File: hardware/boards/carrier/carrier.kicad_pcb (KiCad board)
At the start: 4 copper layers, 106 x 34.3 mm, 50 parts, among them J1 XT30PW(2+2), Q1 IPB020N10N5LF, Q2 2N7002, Q3 2N7002, U1 STM32G031G6U6, U2 LM5163DDAR, U3 LMX5069MS, U4 INA237AIDGSR

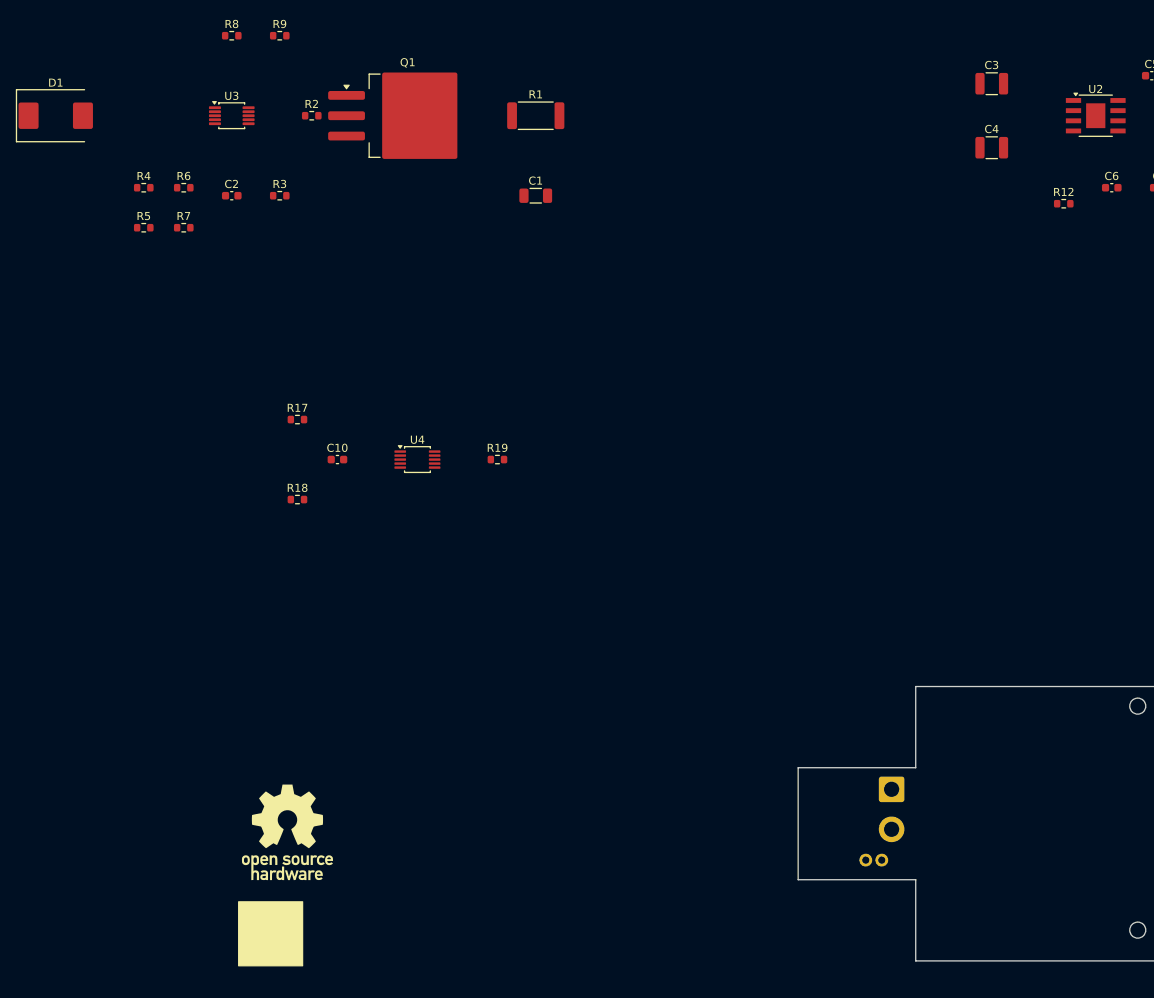
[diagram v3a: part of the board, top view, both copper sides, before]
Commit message: hardware: place carrier input protection and hot-swap
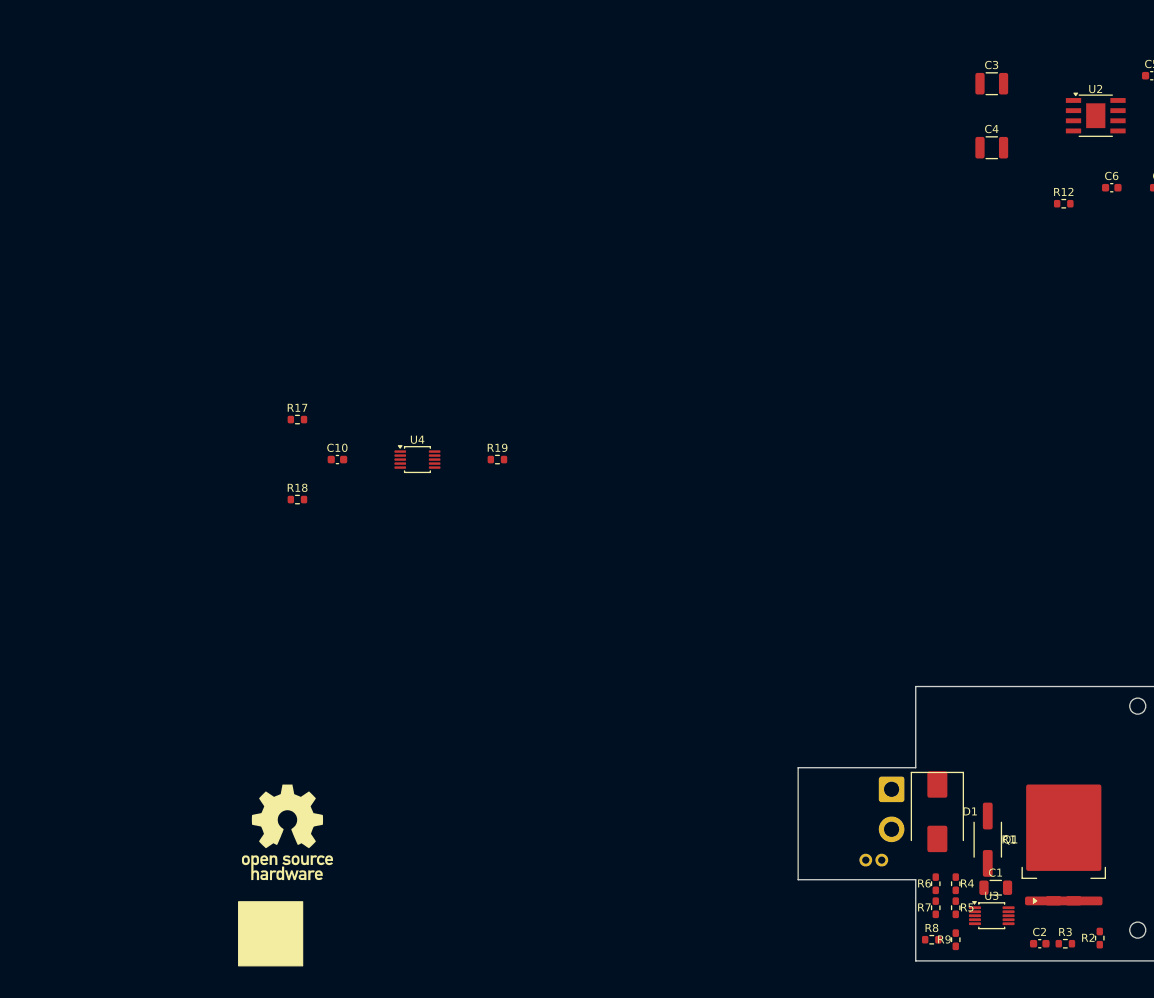
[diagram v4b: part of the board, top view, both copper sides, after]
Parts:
- moved R8 142.9 mm to (117.5, 128.0)
- moved R2 142.4 mm to (138.5, 127.8), turned to 90 degrees
- moved R9 141.1 mm to (120.5, 128.0), turned to 90 degrees
- moved D1 140.4 mm to (118.2, 112.0), turned to -90 degrees
- moved U3 137.9 mm to (125.0, 125.0)
- moved C2 137.6 mm to (131.0, 128.5)
- moved R3 135.6 mm to (134.2, 128.5)
- moved R4 133.7 mm to (120.5, 121.0), turned to -90 degrees
- moved R5 132.4 mm to (120.5, 124.0), turned to -90 degrees
- moved R6 128.1 mm to (118.0, 121.0), turned to 90 degrees
- moved R7 126.7 mm to (118.0, 124.0), turned to 90 degrees
- moved Q1 122.1 mm to (134.0, 115.5), turned to 90 degrees
- moved R1 106.7 mm to (124.5, 115.5), turned to -90 degrees
- moved C1 103.9 mm to (125.5, 121.5)
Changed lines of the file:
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@@
 	(footprint "Resistor_SMD:R_0603_1608Metric"
 		(layer "F.Cu")
-		(at 36 35)
+		(at 134.2 128.5)
 		(descr "Resistor SMD 0603 (1608 Metric), square (rectangular) end terminal, IPC-7351 nominal, (Body size source: IPC-SM-782 page 72, https://www.pcb-3d.com/wordpress/wp-content/uploads/ipc-sm-782a_amendment_1_and_2.pdf)")
 		(tags "resistor")
@@
 	(footprint "Resistor_SMD:R_0603_1608Metric"
 		(layer "F.Cu")
-		(at 40 25)
+		(at 138.5 127.8 90)
 		(descr "Resistor SMD 0603 (1608 Metric), square (rectangular) end terminal, IPC-7351 nominal, (Body size source: IPC-SM-782 page 72, https://www.pcb-3d.com/wordpress/wp-content/uploads/ipc-sm-782a_amendment_1_and_2.pdf)")
 		(tags "resistor")
@@
 	(footprint "Resistor_SMD:R_0603_1608Metric"
 		(layer "F.Cu")
-		(at 30 15)
+		(at 117.5 128)
 		(descr "Resistor SMD 0603 (1608 Metric), square (rectangular) end terminal, IPC-7351 nominal, (Body size source: IPC-SM-782 page 72, https://www.pcb-3d.com/wordpress/wp-content/uploads/ipc-sm-782a_amendment_1_and_2.pdf)")
 		(tags "resistor")
@@
 	(footprint "Package_SO:MSOP-10_3x3mm_P0.5mm"
 		(layer "F.Cu")
-		(at 30 25)
+		(at 125 125)
 		(descr "MSOP, 10 Pin (JEDEC MO-187 variation BA, 0.85mm body thickness, https://www.jedec.org/system/files/docs/mo-187F.pdf)")
 		(tags "MSOP SO TSSOP-10_3x3mm_P0.5mm")
@@
 	(footprint "Capacitor_SMD:C_1206_3216Metric"
 		(layer "F.Cu")
-		(at 68 35)
+		(at 125.5 121.5)
 		(descr "Capacitor SMD 1206 (3216 Metric), square (rectangular) end terminal, IPC-7351 nominal, (Body size source: IPC-SM-782 page 76, https://www.pcb-3d.com/wordpress/wp-content/uploads/ipc-sm-782a_amendment_1_and_2.pdf)")
 		(tags "capacitor")
@@
 	(footprint "Resistor_SMD:R_0603_1608Metric"
 		(layer "F.Cu")
-		(at 24 39)
+		(at 118 124 90)
 		(descr "Resistor SMD 0603 (1608 Metric), square (rectangular) end terminal, IPC-7351 nominal, (Body size source: IPC-SM-782 page 72, https://www.pcb-3d.com/wordpress/wp-content/uploads/ipc-sm-782a_amendment_1_and_2.pdf)")
 		(tags "resistor")
@@
 	(footprint "Resistor_SMD:R_0603_1608Metric"
 		(layer "F.Cu")
-		(at 36 15)
+		(at 120.5 128 90)
 		(descr "Resistor SMD 0603 (1608 Metric), square (rectangular) end terminal, IPC-7351 nominal, (Body size source: IPC-SM-782 page 72, https://www.pcb-3d.com/wordpress/wp-content/uploads/ipc-sm-782a_amendment_1_and_2.pdf)")
 		(tags "resistor")
@@
 	(footprint "Resistor_SMD:R_0603_1608Metric"
 		(layer "F.Cu")
-		(at 19 34)
+		(at 120.5 121 -90)
 		(descr "Resistor SMD 0603 (1608 Metric), square (rectangular) end terminal, IPC-7351 nominal, (Body size source: IPC-SM-782 page 72, https://www.pcb-3d.com/wordpress/wp-content/uploads/ipc-sm-782a_amendment_1_and_2.pdf)")
 		(tags "resistor")
@@
 	(footprint "Resistor_SMD:R_0603_1608Metric"
 		(layer "F.Cu")
-		(at 19 39)
+		(at 120.5 124 -90)
 		(descr "Resistor SMD 0603 (1608 Metric), square (rectangular) end terminal, IPC-7351 nominal, (Body size source: IPC-SM-782 page 72, https://www.pcb-3d.com/wordpress/wp-content/uploads/ipc-sm-782a_amendment_1_and_2.pdf)")
 		(tags "resistor")
@@
 	(footprint "Resistor_SMD:R_0603_1608Metric"
 		(layer "F.Cu")
-		(at 24 34)
+		(at 118 121 90)
 		(descr "Resistor SMD 0603 (1608 Metric), square (rectangular) end terminal, IPC-7351 nominal, (Body size source: IPC-SM-782 page 72, https://www.pcb-3d.com/wordpress/wp-content/uploads/ipc-sm-782a_amendment_1_and_2.pdf)")
 		(tags "resistor")
@@
 	(footprint "Resistor_SMD:R_2512_6332Metric"
 		(layer "F.Cu")
-		(at 68 25)
+		(at 124.5 115.5 -90)
 		(descr "Resistor SMD 2512 (6332 Metric), square (rectangular) end terminal, IPC-7351 nominal, (Body size source: IPC-SM-782 page 72, https://www.pcb-3d.com/wordpress/wp-content/uploads/ipc-sm-782a_amendment_1_and_2.pdf)")
 		(tags "resistor")
@@
 	(footprint "Package_TO_SOT_SMD:TO-263-3_TabPin2"
 		(layer "F.Cu")
-		(at 52 25)
+		(at 134 115.5 90)
 		(descr "TO-263/D2PAK/DDPAK SMD package, http://www.infineon.com/cms/en/product/packages/PG-TO263/PG-TO263-3-1/")
 		(tags "D2PAK DDPAK TO-263 D2PAK-3 TO-263-3 SOT-404")
@@
 	(footprint "Diode_SMD:D_SMC"
 		(layer "F.Cu")
-		(at 8 25)
+		(at 118.2 112 -90)
 		(descr "Diode SMC (DO-214AB)")
 		(tags "Diode SMC (DO-214AB)")
@@
 	(footprint "Capacitor_SMD:C_0603_1608Metric"
 		(layer "F.Cu")
-		(at 30 35)
+		(at 131 128.5)
 		(descr "Capacitor SMD 0603 (1608 Metric), square (rectangular) end terminal, IPC-7351 nominal, (Body size source: IPC-SM-782 page 76, https://www.pcb-3d.com/wordpress/wp-content/uploads/ipc-sm-782a_amendment_1_and_2.pdf)")
 		(tags "capacitor")

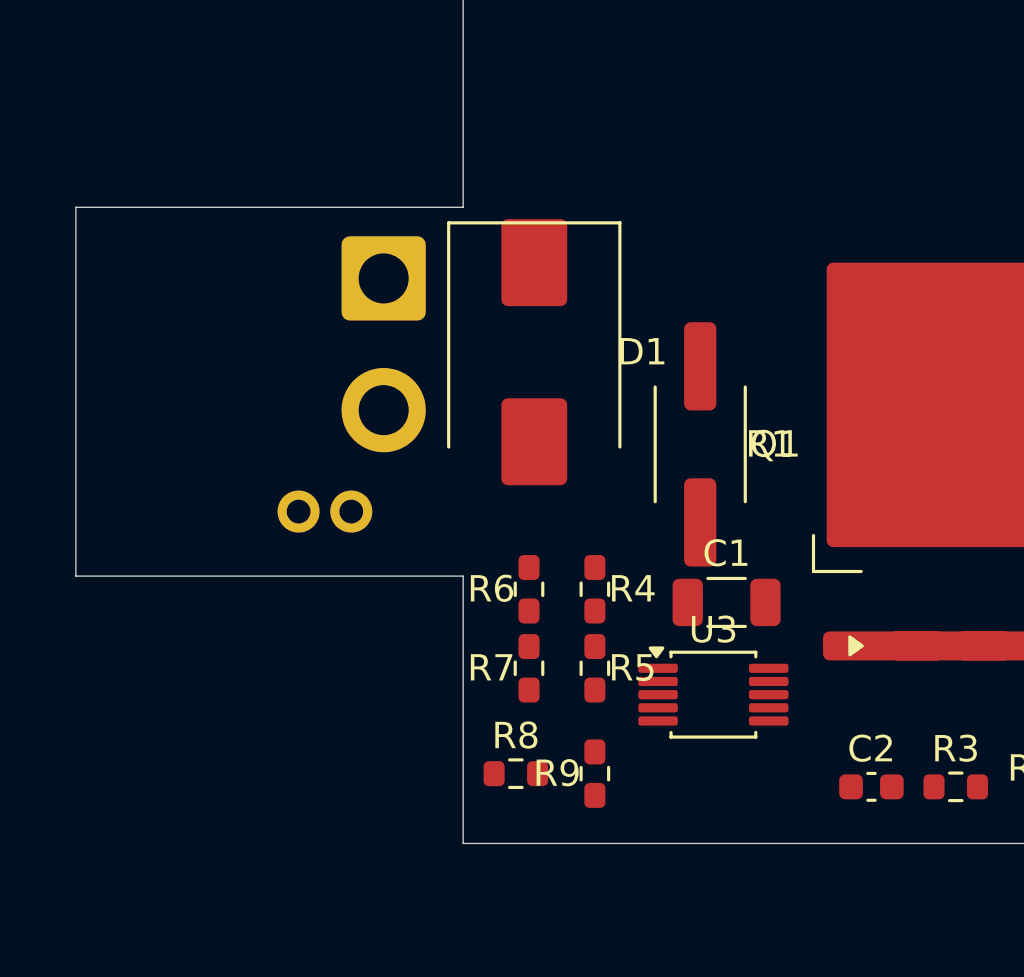
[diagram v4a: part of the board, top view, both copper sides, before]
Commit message: Checkpoint: working on new carrier PCB layout
Not anywhere near done...
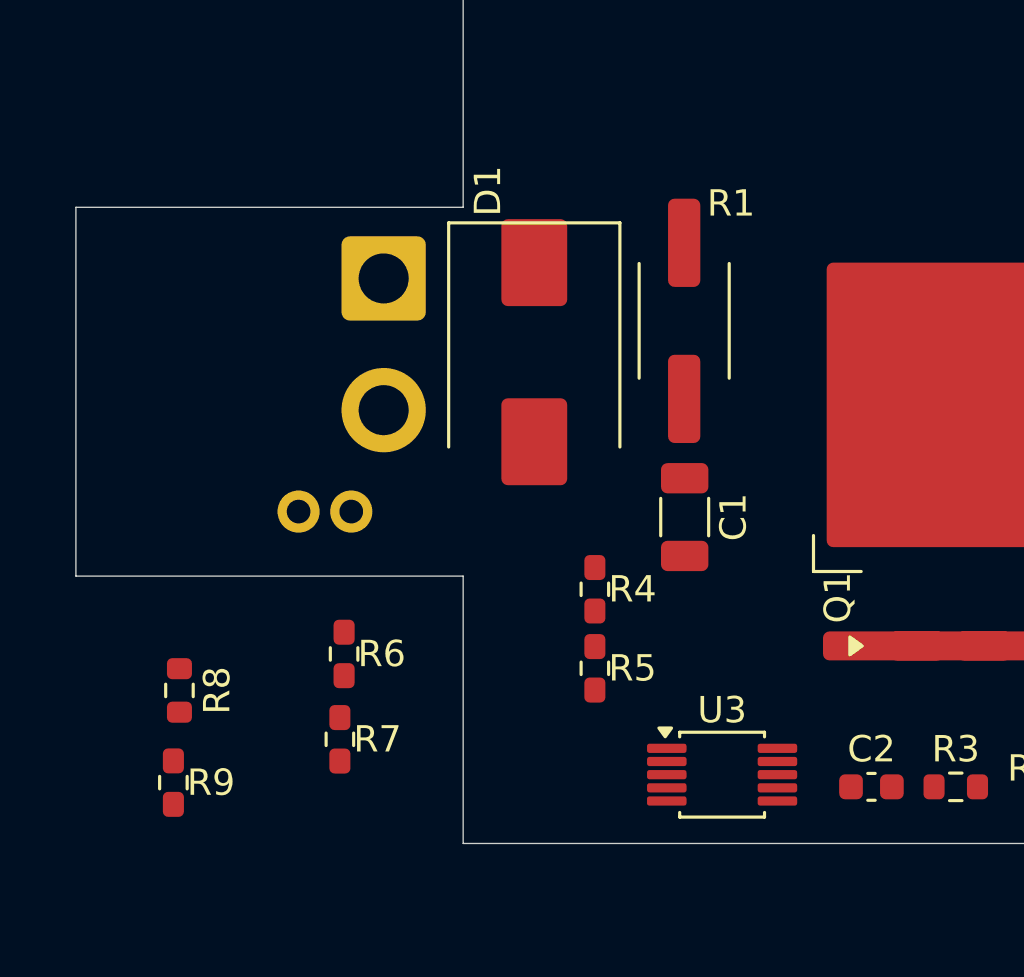
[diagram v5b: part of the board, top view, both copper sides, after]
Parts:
- moved R9 16.0 mm to (104.5, 128.3), turned to -90 degrees
- moved R8 13.2 mm to (104.7, 124.8), turned to -90 degrees
- moved R7 7.67 mm to (110.8, 126.7), turned to -90 degrees
- moved R6 7.44 mm to (111.0, 123.5), turned to -90 degrees
- moved R1 4.73 mm to (123.9, 110.8)
- moved C1 3.61 mm to (123.9, 118.3), turned to -90 degrees
- moved U3 3.06 mm to (125.3, 128.0)

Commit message: checkpoint: save carrier board state
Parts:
- moved R17 59.5 mm to (91.0, 90.5), turned to 90 degrees
- moved R18 58.2 mm to (91.0, 97.5), turned to 90 degrees
- moved C10 54.5 mm to (91.2, 94.0), turned to -90 degrees
- moved R19 54.5 mm to (111.2, 94.0), turned to 90 degrees
- moved U4 54.5 mm to (101.2, 94.0)
- moved C6 21.3 mm to (148.0, 14.3), turned to 90 degrees
- moved C7 16.3 mm to (148.0, 17.8), turned to -90 degrees
- moved R16 16.0 mm to (152.0, 35.5), turned to -90 degrees
- moved C8 15.9 mm to (160.5, 35.0), turned to -90 degrees
- moved R13 15.0 mm to (147.0, 35.5), turned to -90 degrees
- moved R14 14.6 mm to (148.0, 21.9), turned to -90 degrees
- moved R8 14.2 mm to (118.5, 121.2)
- moved R9 14.2 mm to (118.3, 124.7)
- moved C5 13.9 mm to (139.5, 32.7), turned to 90 degrees
- moved R15 13.5 mm to (139.5, 37.2), turned to -90 degrees
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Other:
- board text removed: "INPUT PROTECTION + HOT-SWAP D1, U3, Q1, R1-R9, C1-C2"
- board text removed: "POWER / CURRENT MONITOR U4, C10, R17-R19"
